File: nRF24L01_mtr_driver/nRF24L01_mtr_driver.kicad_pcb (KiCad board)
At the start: 2 copper layers, 64.8 x 45 mm, 140 parts, among them J1 Micro USB, J2 I/O, J4 VBAT, J5 MTR, J6 SERVO, J7 ICSP, Q1 AO4484, Q2 AO4484, Q3 AO4484, Q4 AO4484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

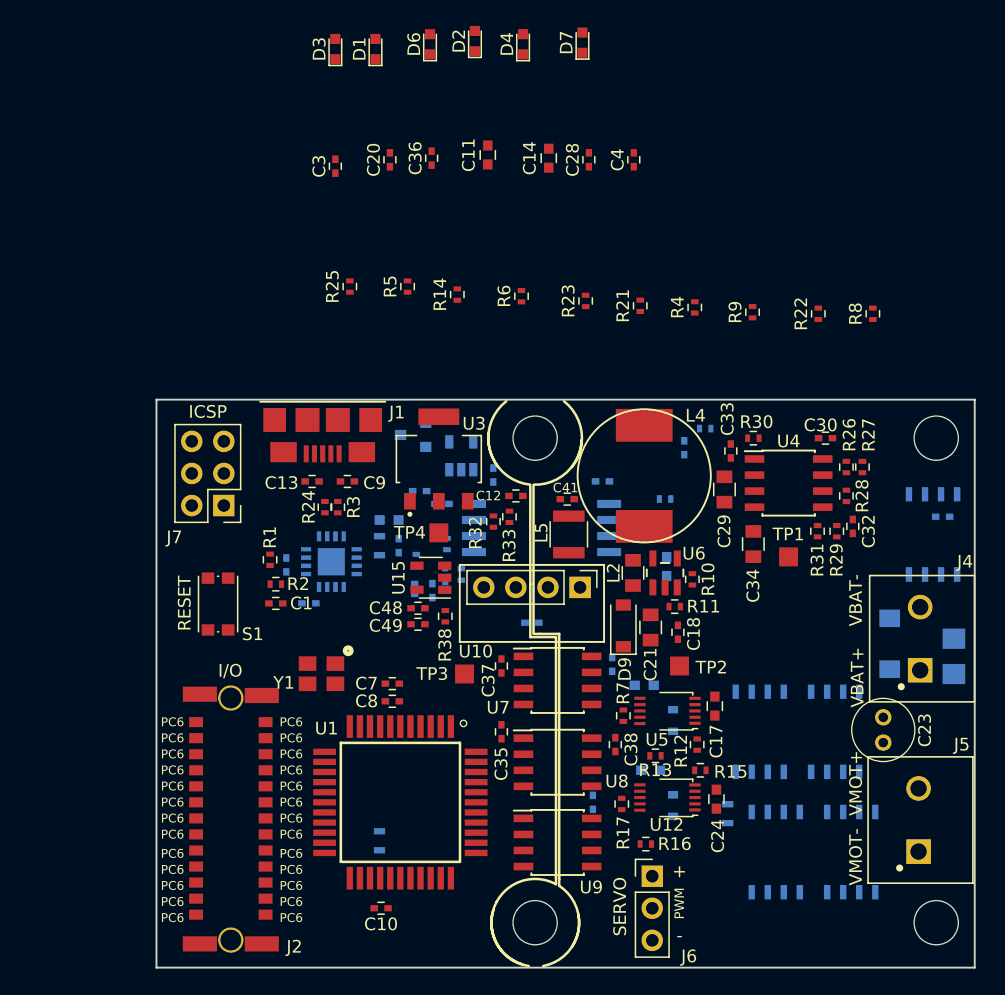
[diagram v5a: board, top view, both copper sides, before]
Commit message: arranged silkscreen, started rounting (ftdi)
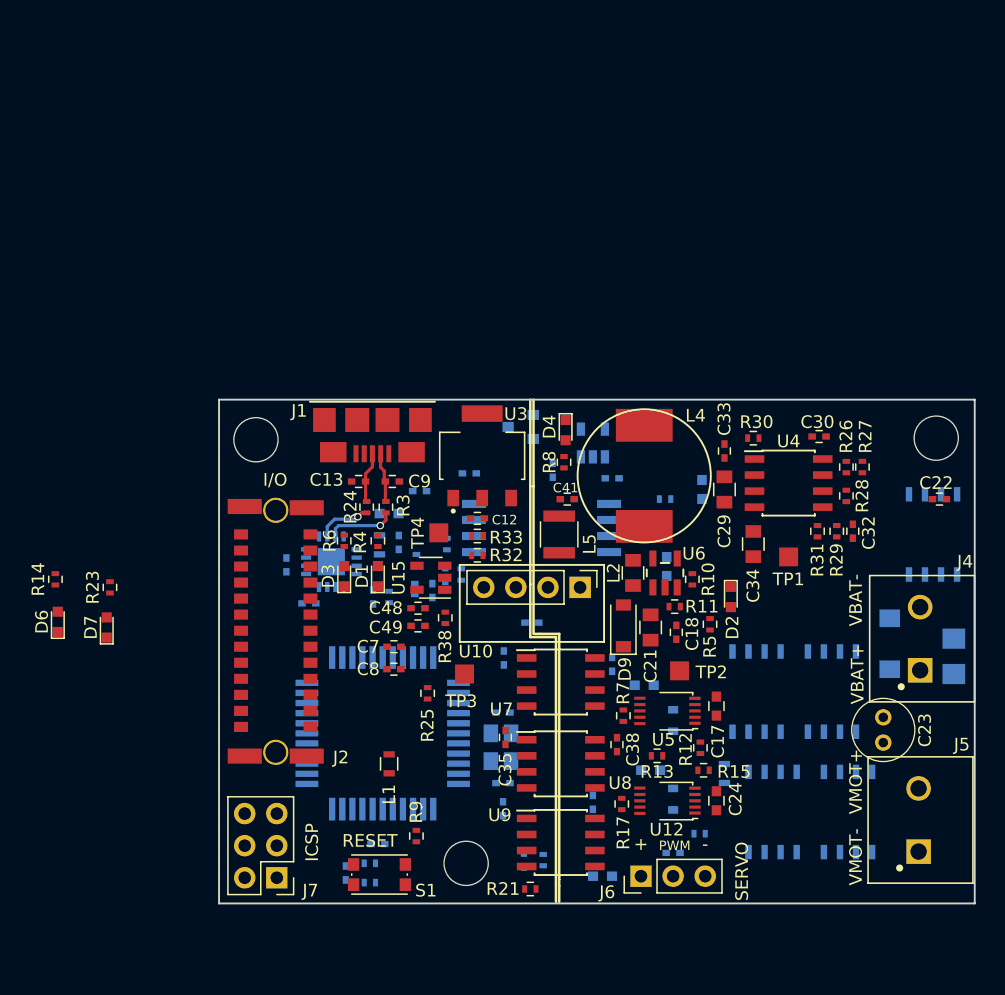
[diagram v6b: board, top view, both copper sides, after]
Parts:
- removed the REF** at (118.0, 86.4)
- C1, C10, C11, C14, C20, C28, C3, C36, C37, C4, R1, R16, R2, R22, U1, Y1: moved to B.Cu
- C22, L1: moved to F.Cu
- R8: value q1k -> 1k
- moved D7 59.7 mm to (52.3, 63.0)
- moved C20 59.3 mm to (97.2, 80.8), turned to 0 degrees
- moved C11 57.8 mm to (91.6, 82.7), turned to 180 degrees
- moved C28 55.7 mm to (85.3, 81.4)
- moved D6 54.4 mm to (48.5, 62.5)
- moved C36 51.8 mm to (83.7, 77.3), turned to 270 degrees
- moved C4 50.4 mm to (83.7, 75.3), turned to 180 degrees
- moved R9 49.3 mm to (76.8, 79.5), turned to 270 degrees
- moved D2 48.4 mm to (101.7, 60.6), turned to 270 degrees
- moved R22 48.4 mm to (86.9, 81.4), turned to 270 degrees
- moved R21 47.0 mm to (85.9, 83.7), turned to 180 degrees
- moved C3 45.2 mm to (83.7, 69.7), turned to 180 degrees
- moved R23 44.0 mm to (52.6, 59.8)
- moved D3 41.7 mm to (71.1, 58.9)
- moved D1 41.7 mm to (73.8, 58.9)
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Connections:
- R4 pad 1: /VBAT_S -> 5V0_MCU
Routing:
- net Net-(R3-Pad1): track 0.00 -> 5.46 mm, vias 0 -> 1
- net Net-(R24-Pad1): track 0.00 -> 4.35 mm, vias 0 -> 1
- net /D+: track 0.00 -> 4.03 mm
- net /D-: track 0.00 -> 3.95 mm
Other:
- board size 64.8 x 45 mm -> 59.8 x 39.9 mm
- board text removed: "PC6"

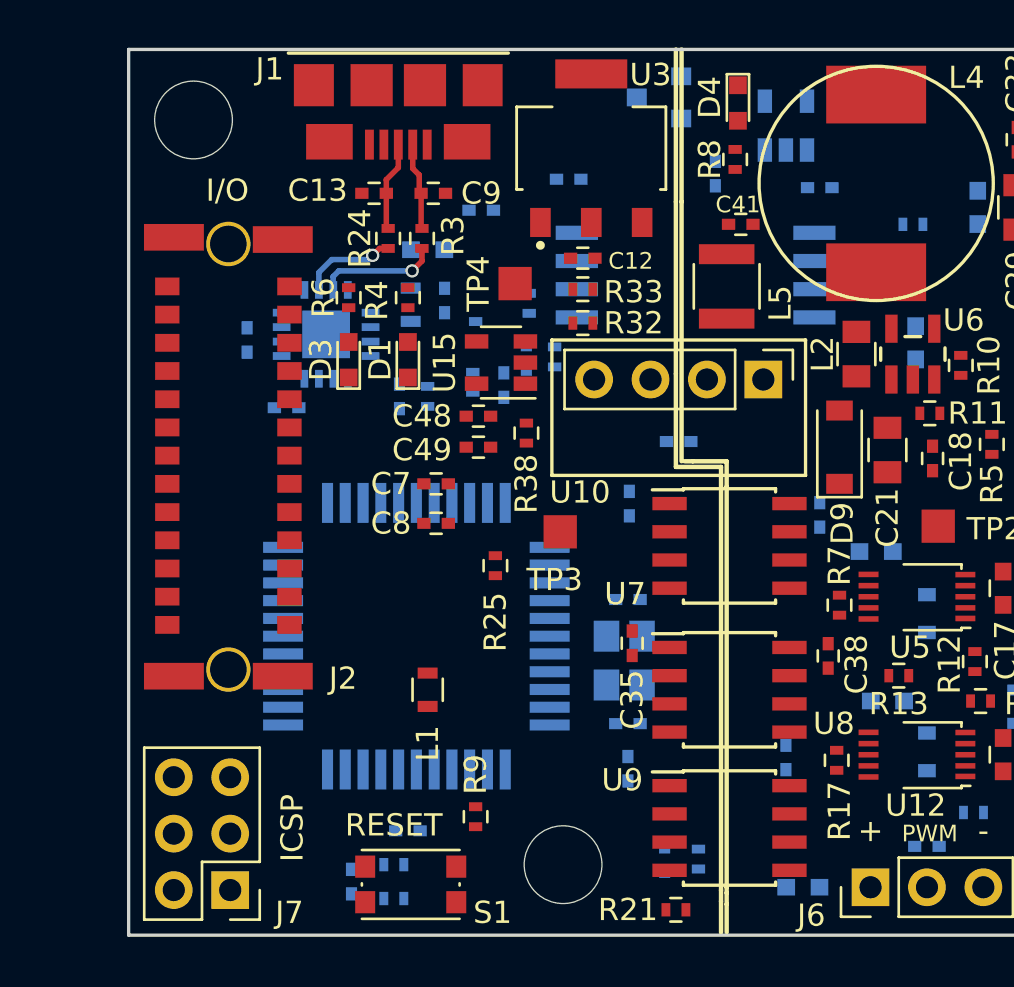
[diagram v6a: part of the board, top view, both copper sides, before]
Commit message: ready for 2 or 4 layer implementation
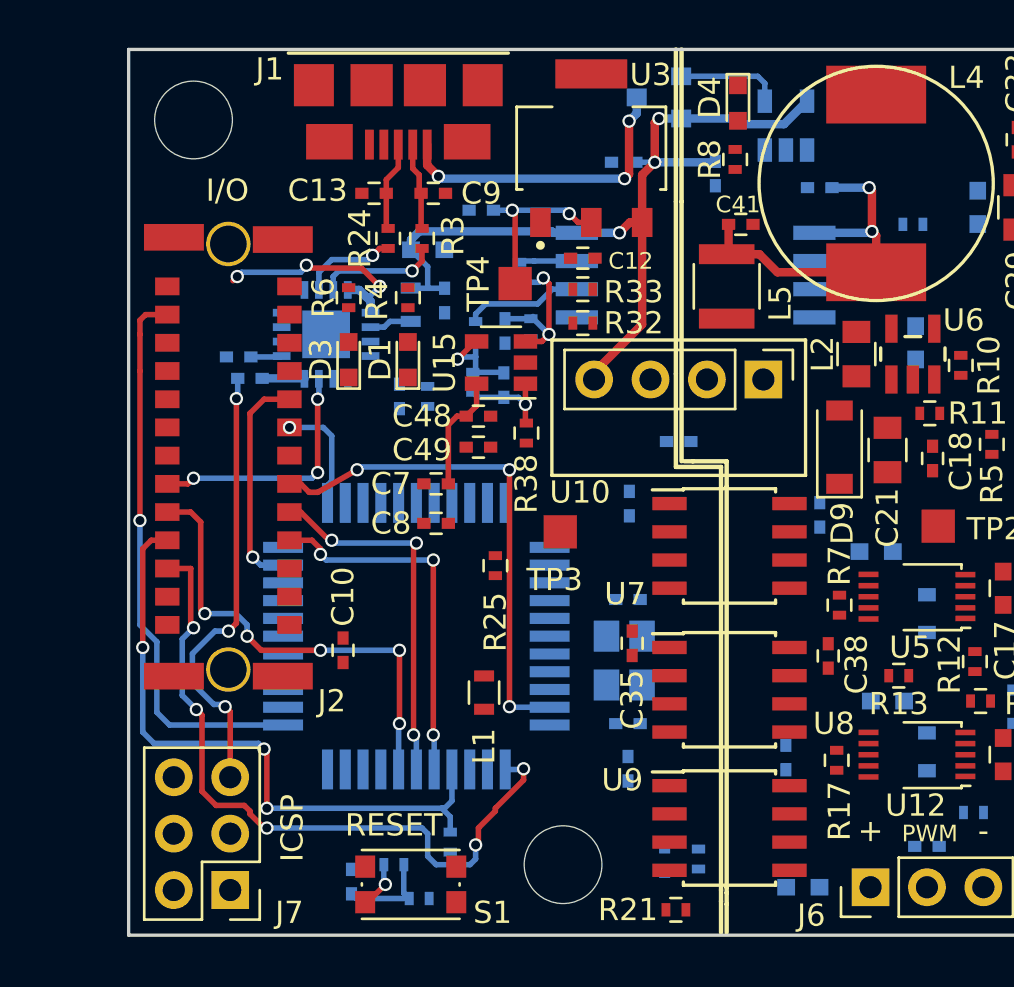
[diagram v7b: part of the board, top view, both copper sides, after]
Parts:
- C10: moved to F.Cu
- R9: moved to B.Cu
- moved C10 8.64 mm to (70.9, 72.0), turned to 90 degrees
- moved C45 2.59 mm to (83.5, 50.0)
- moved L1 2.54 mm to (77.2, 73.9)
- moved C31 2.11 mm to (66.7, 59.8)
- moved R36 1.66 mm to (79.3, 57.5)
- moved R9 1.62 mm to (75.7, 80.6), turned to 90 degrees
- moved C46 1.52 mm to (78.2, 57.6)
- moved R35 1.46 mm to (78.8, 55.0)
- moved R1 1.14 mm to (74.3, 83.2), turned to 180 degrees
- moved C6 0.85 mm to (66.2, 58.8), turned to 180 degrees
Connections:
- C48 pad 1: Net-(C48-Pad1) -> 5V0_MCU
- J2 pad 8: /~SS1 -> /~SS1~
- U15 pad 5: Net-(C48-Pad1) -> 5V0_MCU
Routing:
- net 5V0_MCU: track 0.00 -> 43.8 mm, vias 0 -> 3
- net /IRQ: track 0.00 -> 32.0 mm, vias 0 -> 5
- net /~SS1~: track 0.00 -> 29.3 mm, vias 0 -> 3
- net /PC4: track 0.00 -> 25.2 mm, vias 0 -> 1
- net /~RESET: track 0.00 -> 24.4 mm, vias 0 -> 3
- net /TX0: track 0.00 -> 22.9 mm, vias 0 -> 3
- net /MOSI1: track 0.00 -> 21.0 mm, vias 0 -> 5
- net 5V0_PWR: track 0.00 -> 16.7 mm, vias 0 -> 2
- net /MISO1: track 0.00 -> 16.6 mm, vias 0 -> 3
- net /SCK1: track 0.00 -> 16.4 mm, vias 0 -> 3
- net 5V0_USB: track 0.00 -> 13.9 mm, vias 0 -> 3
- net Net-(C6-Pad1): track 0.00 -> 11.3 mm, vias 0 -> 3
- net /RX0: track 0.00 -> 11.2 mm, vias 0 -> 3
- net /ADC5: track 0.00 -> 10.1 mm, vias 0 -> 1
- net 3V3_MCU: track 0.00 -> 7.99 mm, vias 0 -> 2
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
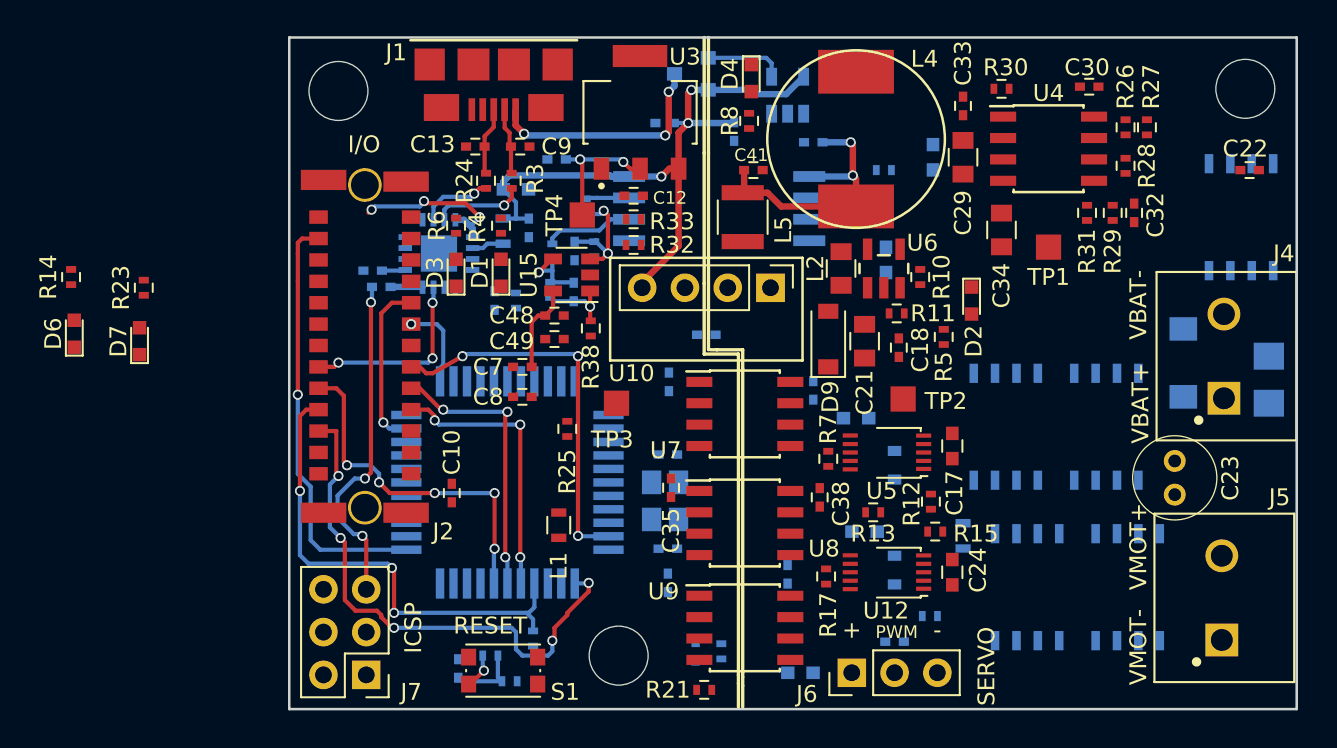
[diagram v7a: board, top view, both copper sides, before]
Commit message: logic side rounting done (4 layer)
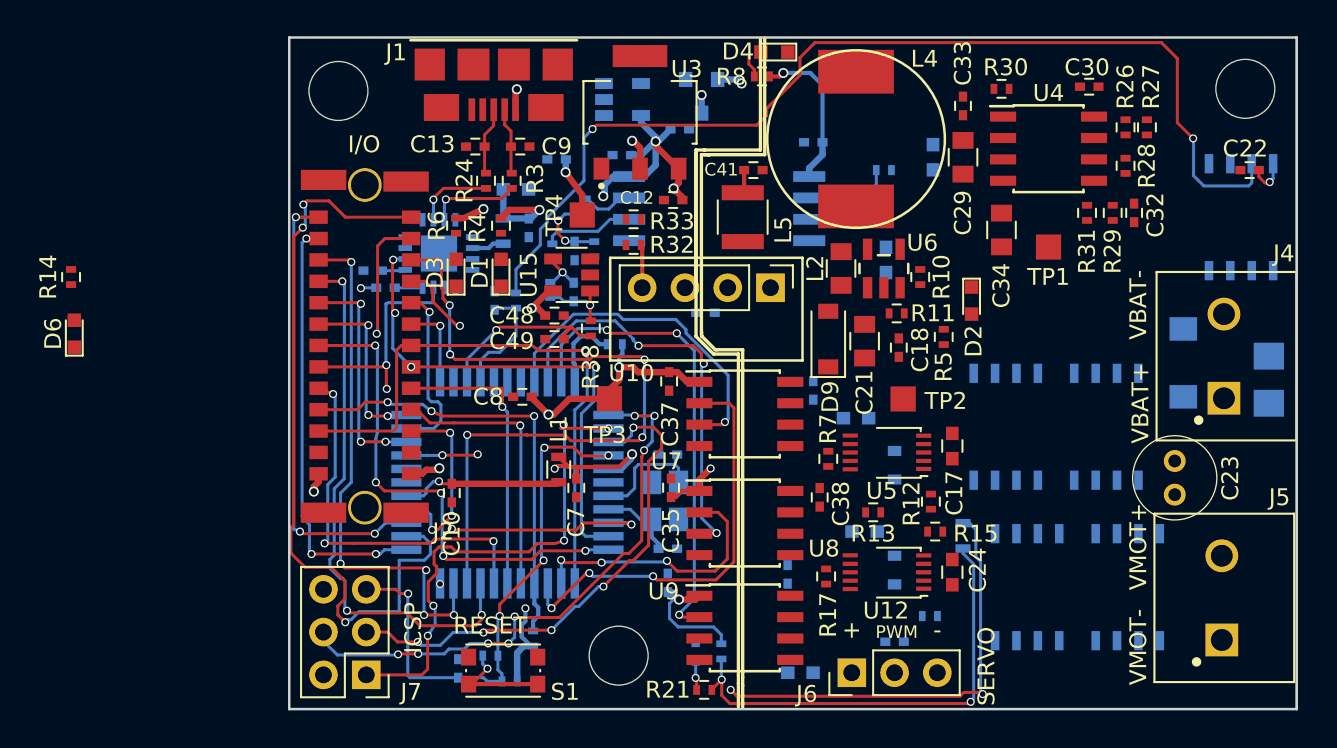
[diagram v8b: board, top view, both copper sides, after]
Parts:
- removed D7: LED, LEDs:LED_0603
- removed R23: 1k, Resistors_SMD:R_0402
- C37: moved to F.Cu
- R25: moved to B.Cu
- moved U11 9.81 mm to (81.0, 48.6), turned to 0 degrees
- moved C7 7.87 mm to (78.3, 71.7), turned to 270 degrees
- moved R25 5.77 mm to (80.5, 63.2), turned to 180 degrees
- moved L1 3.30 mm to (77.2, 70.6), turned to 90 degrees
- moved C43 3.23 mm to (84.4, 50.4), turned to 0 degrees
- moved C45 3.17 mm to (81.0, 51.9)
- moved R8 2.75 mm to (89.3, 47.3), turned to 180 degrees
- moved C12 2.36 mm to (84.0, 54.6), turned to 180 degrees
- moved D4 2.07 mm to (90.0, 45.8), turned to 180 degrees
- moved Q5 1.47 mm to (85.7, 48.5), turned to 270 degrees
- moved C42 1.31 mm to (85.9, 61.3)
- moved TP3 0.50 mm to (80.2, 66.4)
- moved C31 0.26 mm to (66.9, 59.8)
- turned C37 to 90 degrees
- turned C10 to 270 degrees
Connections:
- net /LED2 renamed /MOSI0
- D2 pad 1: GNDA -> GND_PWR
- D4 pad 1: GNDA -> GND_PWR
- R22 pad 1: /5V -> 5V0_MCU
- R25 pad 1: /5V -> 5V0_MCU
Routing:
- net 5V0_MCU: track 43.8 -> 173.5 mm, vias 3 -> 15
- net Net-(R18-Pad2): track 0.00 -> 62.0 mm, vias 0 -> 2
- net /PC5: track 0.00 -> 45.4 mm, vias 0 -> 3
- net /PC1: track 0.00 -> 43.5 mm, vias 0 -> 5
- net /MOSI0: track 0.00 -> 33.8 mm, vias 0 -> 8
- net /PC0: track 0.00 -> 32.6 mm, vias 0 -> 3
- net /PC2: track 0.00 -> 31.8 mm, vias 0 -> 5
- net 3V3_MCU: track 7.99 -> 39.4 mm, vias 2 -> 4
- net /SCK0: track 0.00 -> 30.3 mm, vias 0 -> 5
- net /RX1: track 0.00 -> 29.8 mm, vias 0 -> 5
- net /MISO0: track 0.00 -> 29.5 mm, vias 0 -> 5
- net /PB3: track 0.00 -> 28.3 mm, vias 0 -> 3
- net /~RESET: track 24.4 -> 52.4 mm, vias 3 -> 6
- net Net-(R21-Pad1): track 0.00 -> 27.5 mm, vias 0 -> 2
- net /PC6: track 0.00 -> 27.0 mm, vias 0 -> 3
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- added copper zone on In1.Cu, net 3V3_MCU
- added copper zone on In1.Cu, net 5V0_MCU
- added copper zone on In2.Cu, net GNDA
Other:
- copper layers 2 -> 4
